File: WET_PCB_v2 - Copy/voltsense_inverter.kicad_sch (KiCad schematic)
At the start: 9 parts, among them J17 Capacitor connector, U1 Opamp_Quad

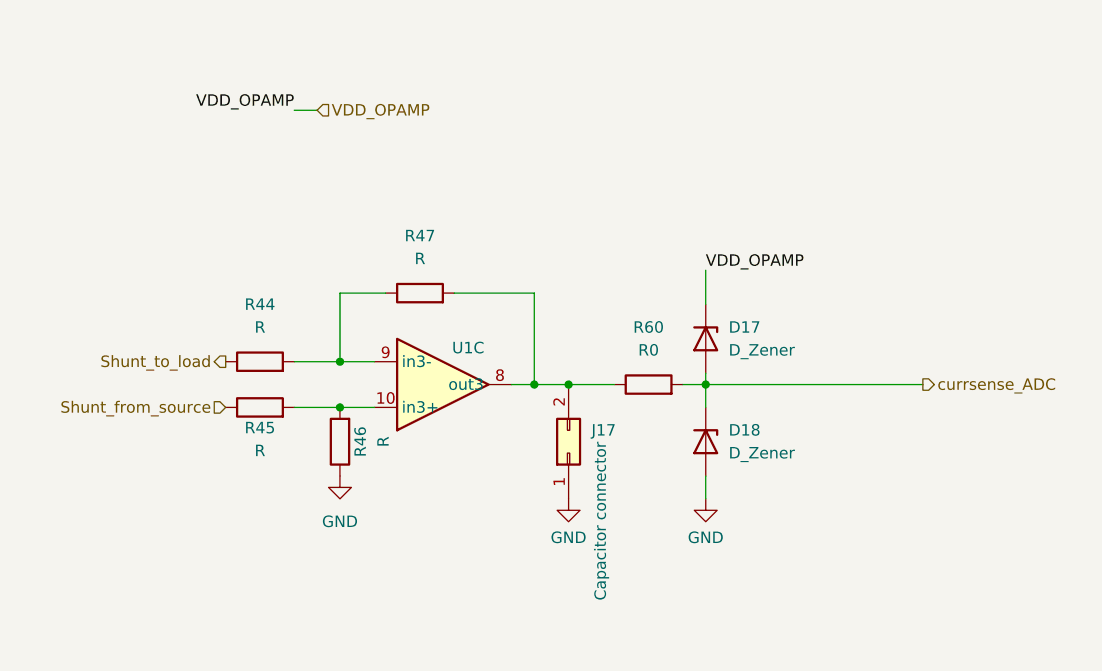
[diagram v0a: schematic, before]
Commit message: microcontroller to chip traces done
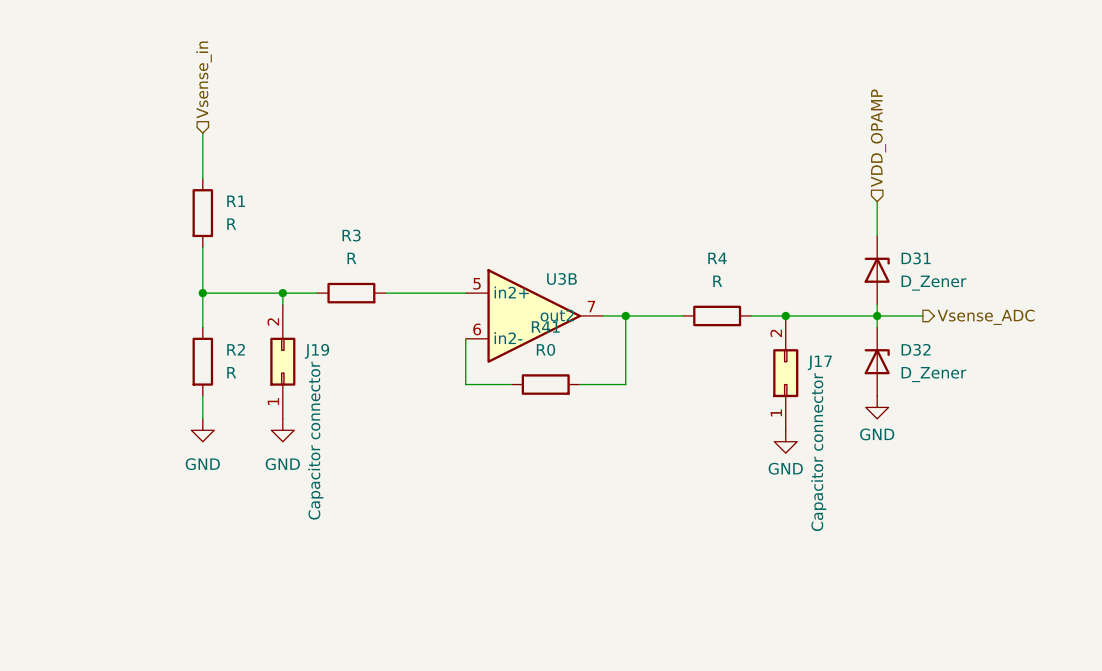
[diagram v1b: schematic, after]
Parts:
- removed D17, D18: D_Zener, Diode_SMD:D_SMF, symbol Device:D_Zener
- removed R44, R45, R46, R47: R, Resistor_SMD:R_0805_2012Metric_Pad1.20x1.40mm_HandSolder, symbol Device:R
- removed R60: R0, Resistor_SMD:R_0805_2012Metric_Pad1.20x1.40mm_HandSolder, symbol Device:R
- removed U1: Opamp_Quad, Package_DIP:DIP-14_W7.62mm, symbol Device:Opamp_Quad
- added D31, D32: D_Zener, Diode_THT:D_DO-15_P2.54mm_Vertical_CathodeUp, symbol Device:D_Zener
- added J19: Capacitor connector, Connector_PinSocket_2.54mm:PinSocket_1x02_P2.54mm_Vertical, symbol Connector_Generic:Conn_02x01
- added R1, R2, R3, R4: R, Resistor_SMD:R_0805_2012Metric_Pad1.20x1.40mm_HandSolder, symbol Device:R
- added R41: R0, Resistor_SMD:R_0805_2012Metric_Pad1.20x1.40mm_HandSolder, symbol Device:R
- added U3: Opamp_Quad, Package_DIP:DIP-14_W7.62mm, symbol Device:Opamp_Quad
- J17: footprint Connector_PinSocket_2.54mm:PinSocket_1x02_P2.54mm_Horizontal -> Connector_PinSocket_2.54mm:PinSocket_1x02_P2.54mm_Vertical
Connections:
- net GND: now also D32.2 (A), J19.1 (Pin_1), R2.2
- net VDD_OPAMP: now also D31.1 (K)
- net Vsense_ADC: now reaches J17.2 (Pin_2)
- net Vsense_ADC: now also D31.2 (A), D32.1 (K), R4.2
- new net: R4.1, R41.2, U3.7 (out2)
- new net: J19.2 (Pin_2), R1.2, R2.1, R3.1
- new net: R3.2, U3.5 (in2+)
- new net: R41.1, U3.6 (in2-)
- new net Vsense_in: R1.1
